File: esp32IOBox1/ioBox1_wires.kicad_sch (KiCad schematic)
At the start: 10 parts, among them J1 M_multimeter12v, J2 M_termometer, J3 Screw_Terminal_01x02, SW1 on / off switch, U1 dc to dc converter set 5v

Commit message: fix thermo module
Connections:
- net 3.3v: no longer J1.1 (Pin_1), J2.1 (Pin_1), R1.2, R2.1
- net GPIO_ADC: now reaches J3.2 (Pin_2), R3.2, R4.2
- net GPIO_ADC: now also J1.1 (Pin_1), J2.1 (Pin_1), R1.2, R2.1
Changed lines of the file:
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@@
 (kicad_sch (version 20230121) (generator eeschema)
   (paper "A4")
-  (junction (at 165.1 135.89) (diameter 0) (color 0 0 0 0)
-  )
   (junction (at 162.56 138.43) (diameter 0) (color 0 0 0 0)
   )
-  (junction (at 162.56 135.89) (diameter 0) (color 0 0 0 0)
+  (junction (at 162.56 93.98) (diameter 0) (color 0 0 0 0)
   )
-  (junction (at 162.56 93.98) (diameter 0) (color 0 0 0 0)
+  (junction (at 176.53 129.54) (diameter 0) (color 0 0 0 0)
   )
   (junction (at 182.88 129.54) (diameter 0) (color 0 0 0 0)
@@
   (junction (at 161.29 140.97) (diameter 0) (color 0 0 0 0)
   )
-  (wire (pts (xy 165.1 127) (xy 165.1 135.89))
-    (stroke (width 0) (type default))
+  (junction (at 162.56 129.54) (diameter 0) (color 0 0 0 0)
   )
   (wire (pts (xy 161.29 149.86) (xy 161.29 140.97))
@@
     (stroke (width 0) (type default))
   )
-  (wire (pts (xy 165.1 135.89) (xy 165.1 138.43))
-    (stroke (width 0) (type default))
-  )
-  (wire (pts (xy 162.56 135.89) (xy 165.1 135.89))
+  (wire (pts (xy 165.1 127) (xy 165.1 138.43))
     (stroke (width 0) (type default))
   )
@@
   )
   (wire (pts (xy 41.91 111.76) (xy 46.99 111.76))
+    (stroke (width 0) (type default))
+  )
+  (wire (pts (xy 162.56 129.54) (xy 176.53 129.54))
     (stroke (width 0) (type default))
   )
@@
     (stroke (width 0) (type default))
   )
+  (wire (pts (xy 162.56 129.54) (xy 162.56 135.89))
+    (stroke (width 0) (type default))
+  )
   (wire (pts (xy 168.91 111.76) (xy 161.29 111.76))
     (stroke (width 0) (type default))
@@
     (stroke (width 0) (type default))
   )
-  (wire (pts (xy 162.56 121.92) (xy 162.56 135.89))
+  (wire (pts (xy 162.56 121.92) (xy 162.56 129.54))
     (stroke (width 0) (type default))
   )

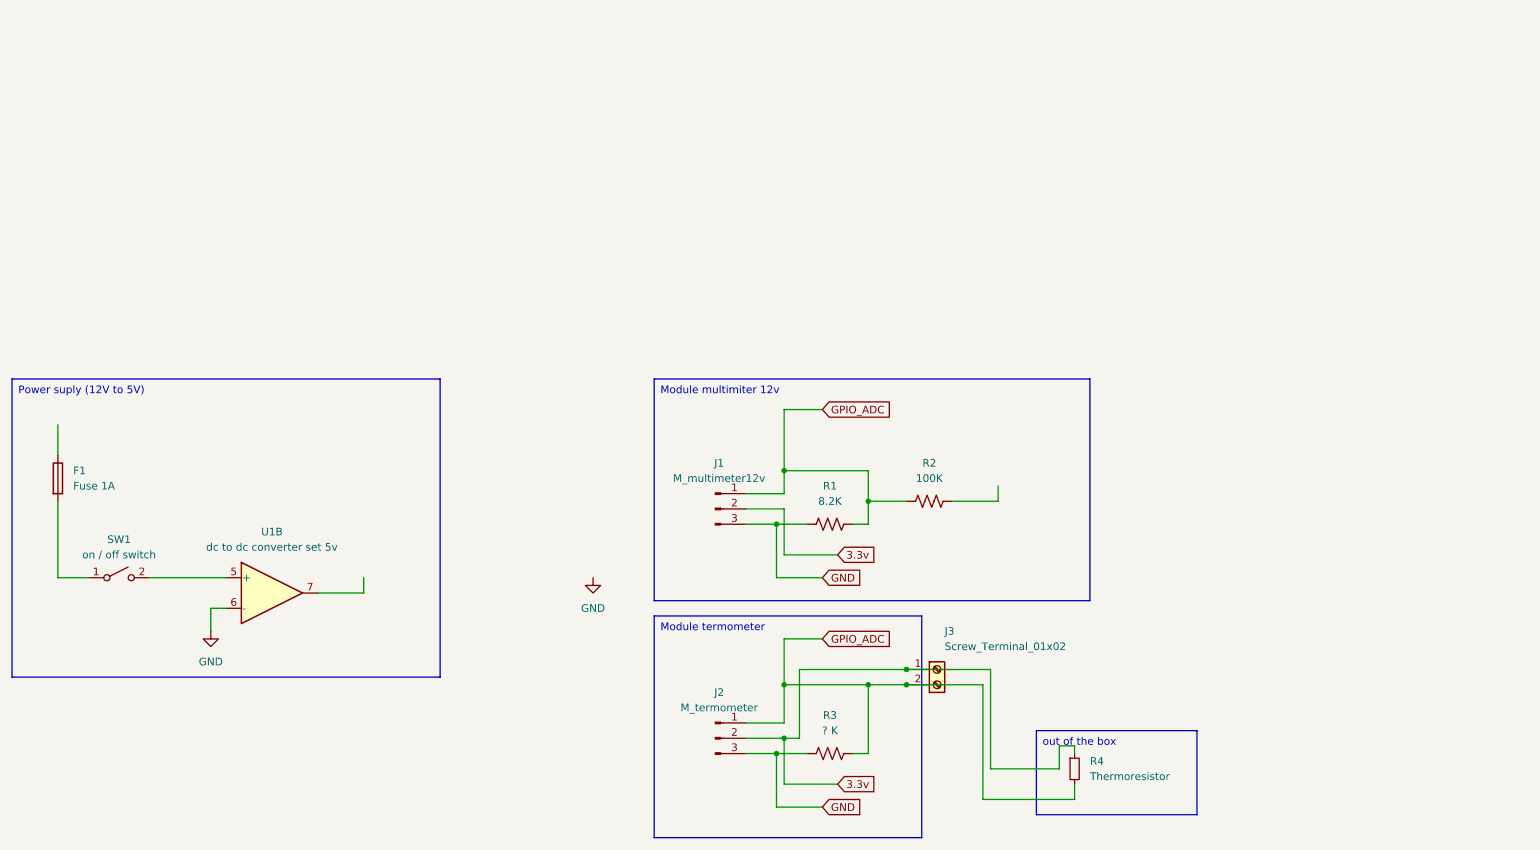
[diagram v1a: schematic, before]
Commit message: yyyyymm push esp32iobox2
+ drawings
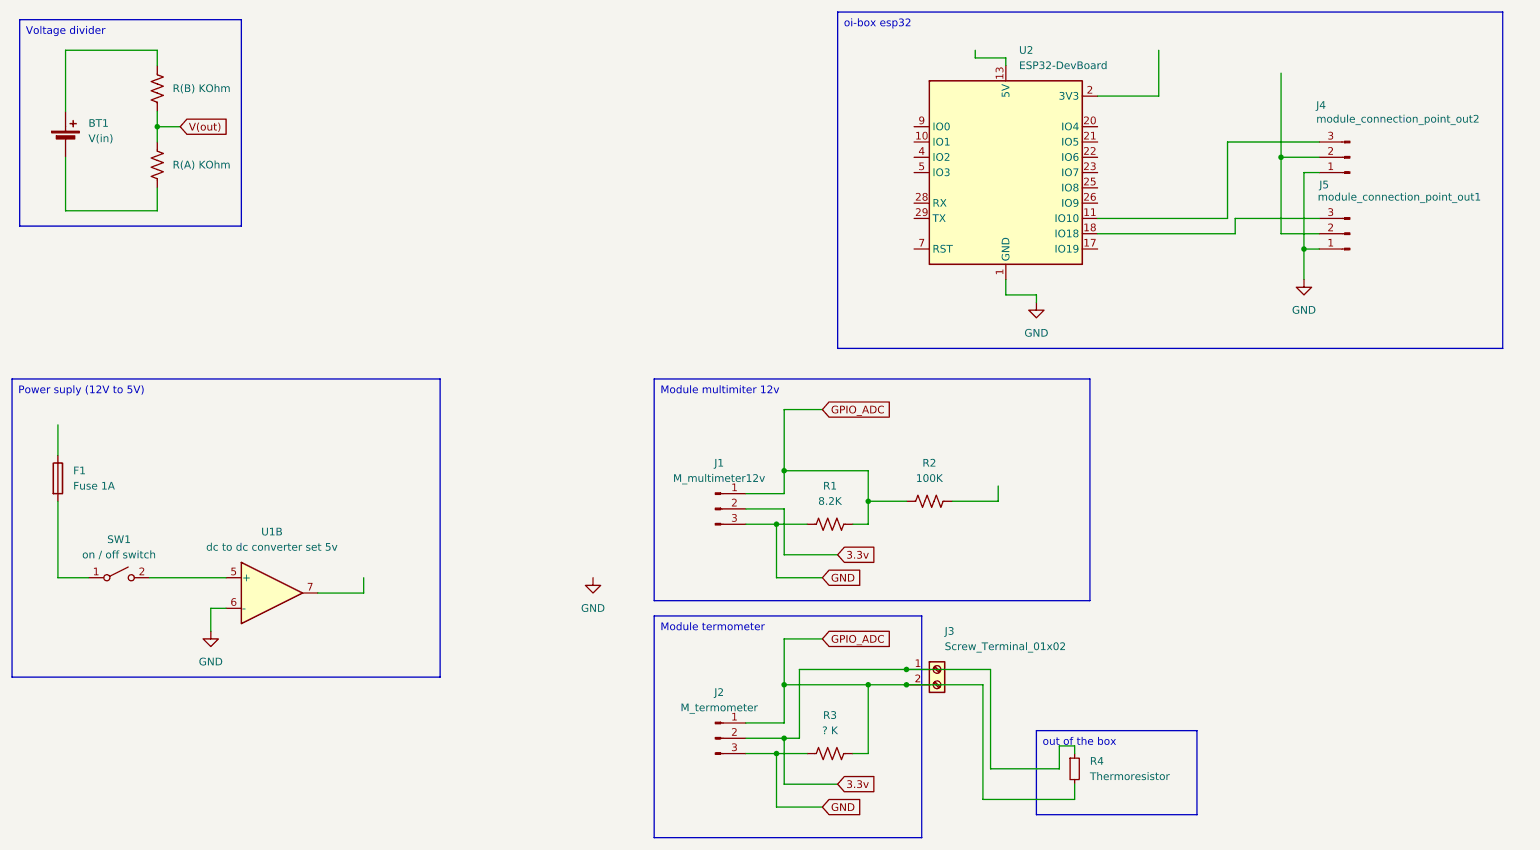
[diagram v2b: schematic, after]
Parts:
- added BT1: V(in), symbol Device:Battery_Cell
- added J4: module_connection_point_out2, symbol Connector:Conn_01x03_Pin
- added J5: module_connection_point_out1, symbol Connector:Conn_01x03_Pin
- added R5: R(B) KOhm, symbol Device:R_US
- added R6: R(A) KOhm, symbol Device:R_US
- added U2: ESP32-DevBoard, RF_Module:ESP32-C3-DevKitM-1, symbol RF_Module:ESP32-C3-DevKitM-1
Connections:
- net GND: now also J4.1 (Pin_1), J5.1 (Pin_1), U2.1 (GND), U2.12 (GND), U2.15 (GND), U2.16 (GND), U2.19 (GND), U2.24 (GND), U2.27 (GND), U2.30 (GND), U2.6 (GND), U2.8 (GND)
- new net: BT1.1 (+), R5.2
- new net: BT1.2 (-), R6.1
- new net: J4.3 (Pin_3), U2.11 (IO10)
- new net: U2.13 (5V), U2.14 (5V)
- new net: J5.3 (Pin_3), U2.18 (IO18)
- new net: U2.2 (3V3), U2.3 (3V3)
- new net: J4.2 (Pin_2), J5.2 (Pin_2)
- new net V(out): R5.1, R6.2
